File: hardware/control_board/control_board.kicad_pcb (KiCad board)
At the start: 2 copper layers, 80 x 80 mm, 126 parts, among them J1 SWD, J2 Aux, J3 Panel, J4 6.5/2mm, J5 USB_C, J6 RTD, J7 TC, J8 Conn_01x01, J9 Conn_01x01, Q1 2N7002A, Q2 IRF1018ESTRLPBF, SW1 Reset, SW2 Power, U1 STM32F103C8T6, U2 LMR38010SDDAR, U3 TLV76133DCYR, U4 USBLC6-2SC6, U5 MAX6675, U6 MCP6N11T-005E, U7 MCP6001T, U8 TLP183, Y1 8MHz

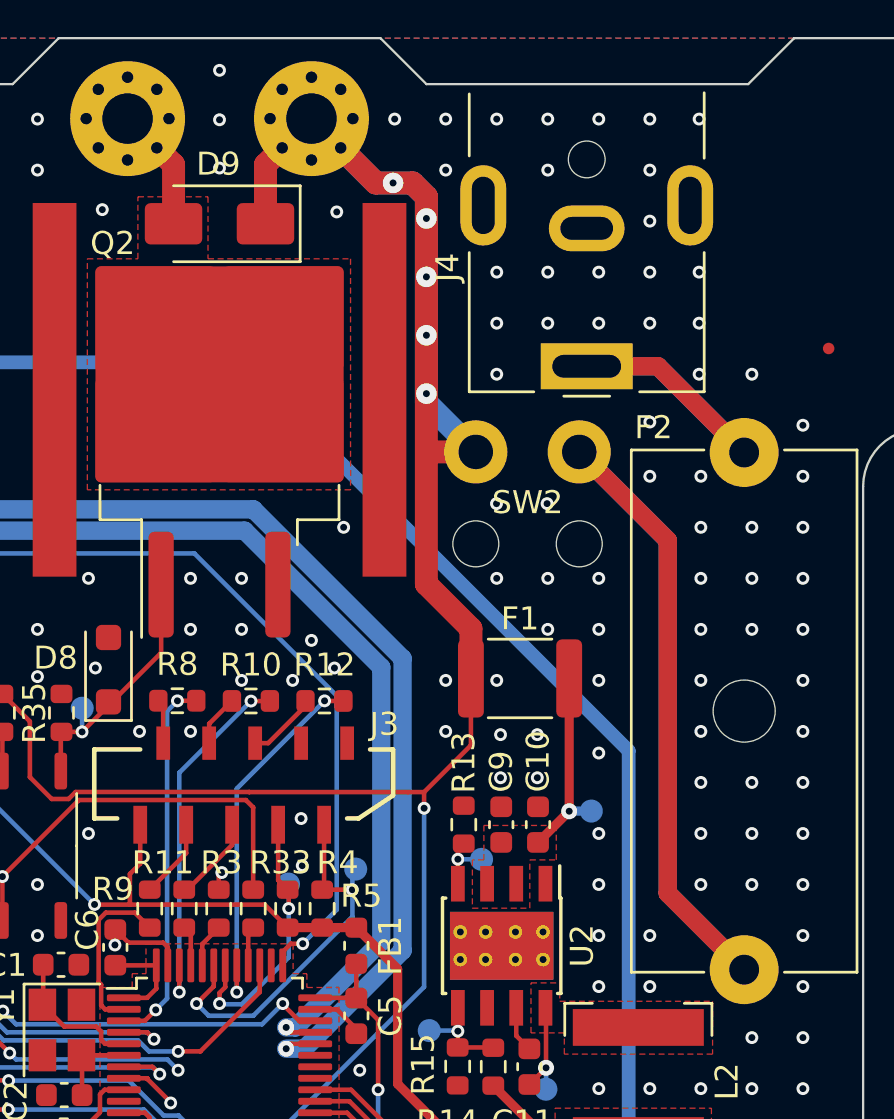
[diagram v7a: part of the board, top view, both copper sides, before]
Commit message: Add vias to the high current tracks
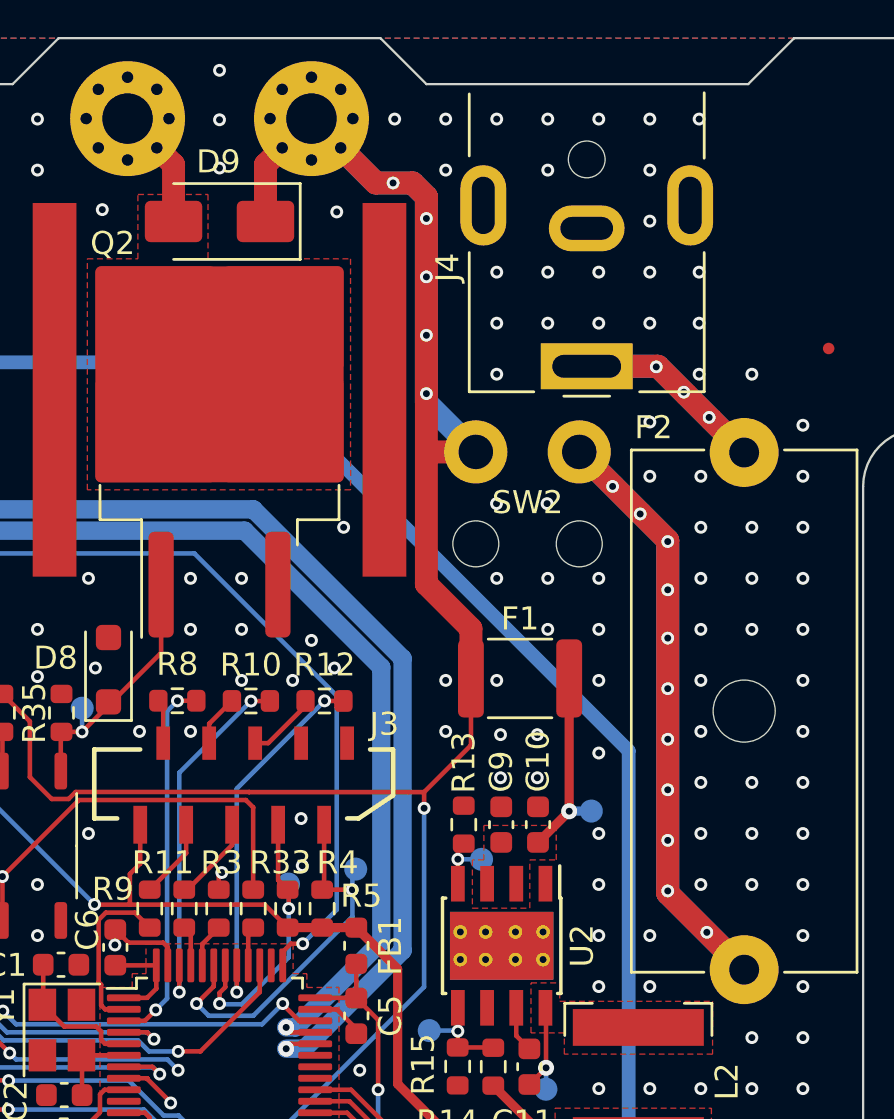
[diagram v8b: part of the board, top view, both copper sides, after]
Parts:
- moved D9 0.10 mm to (148.0, 68.0)
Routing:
- net Net-(SW2-A): track 51.0 -> 50.9 mm, vias 0 -> 11
- net Net-(F2-Pad1): vias 0 -> 3
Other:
- board text added: "20230914"
- board text removed: "20230913"
